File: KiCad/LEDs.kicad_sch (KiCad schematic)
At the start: 36 parts

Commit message: First production
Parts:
- gave numbers to parts that had none: 36

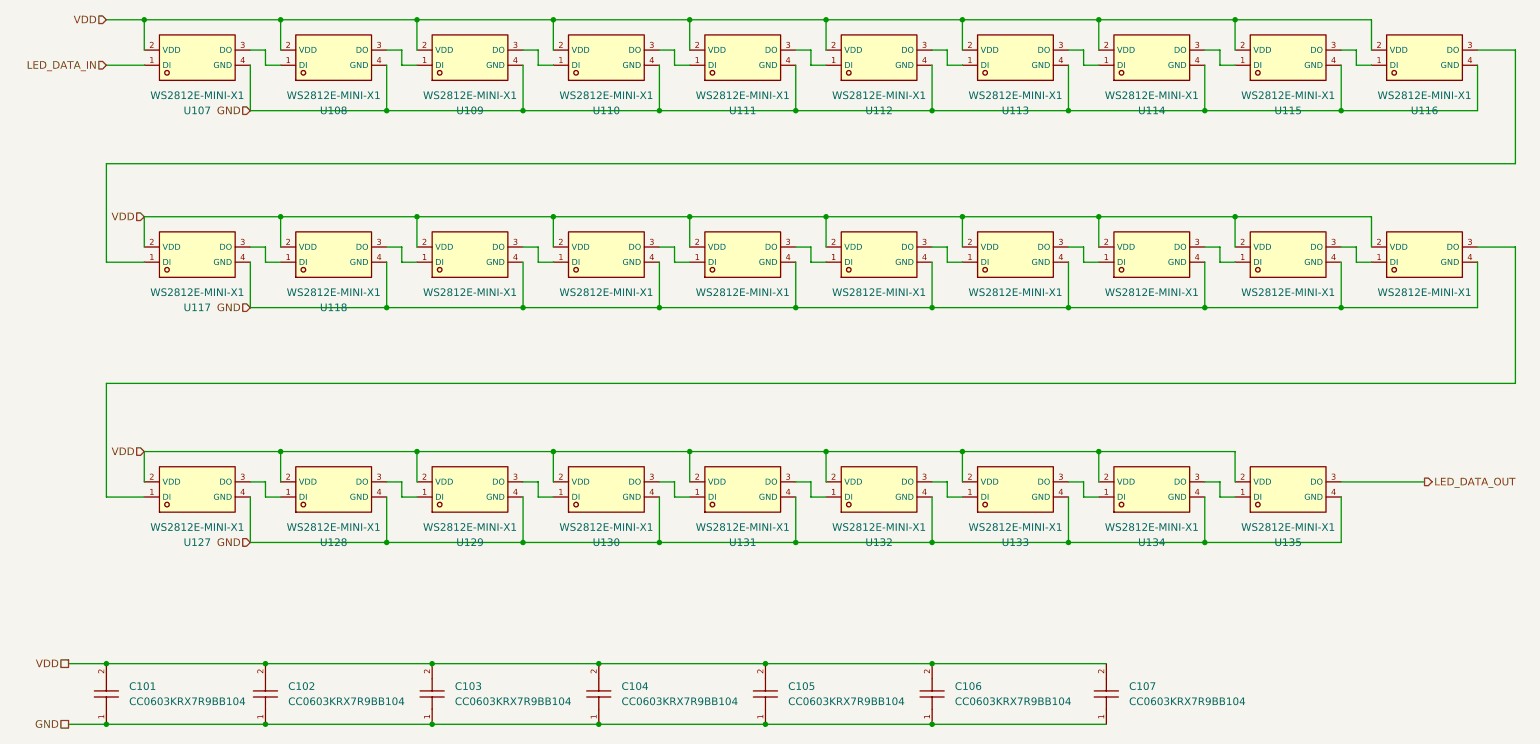
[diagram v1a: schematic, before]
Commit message: Updated to not use adressable LED. Sch only
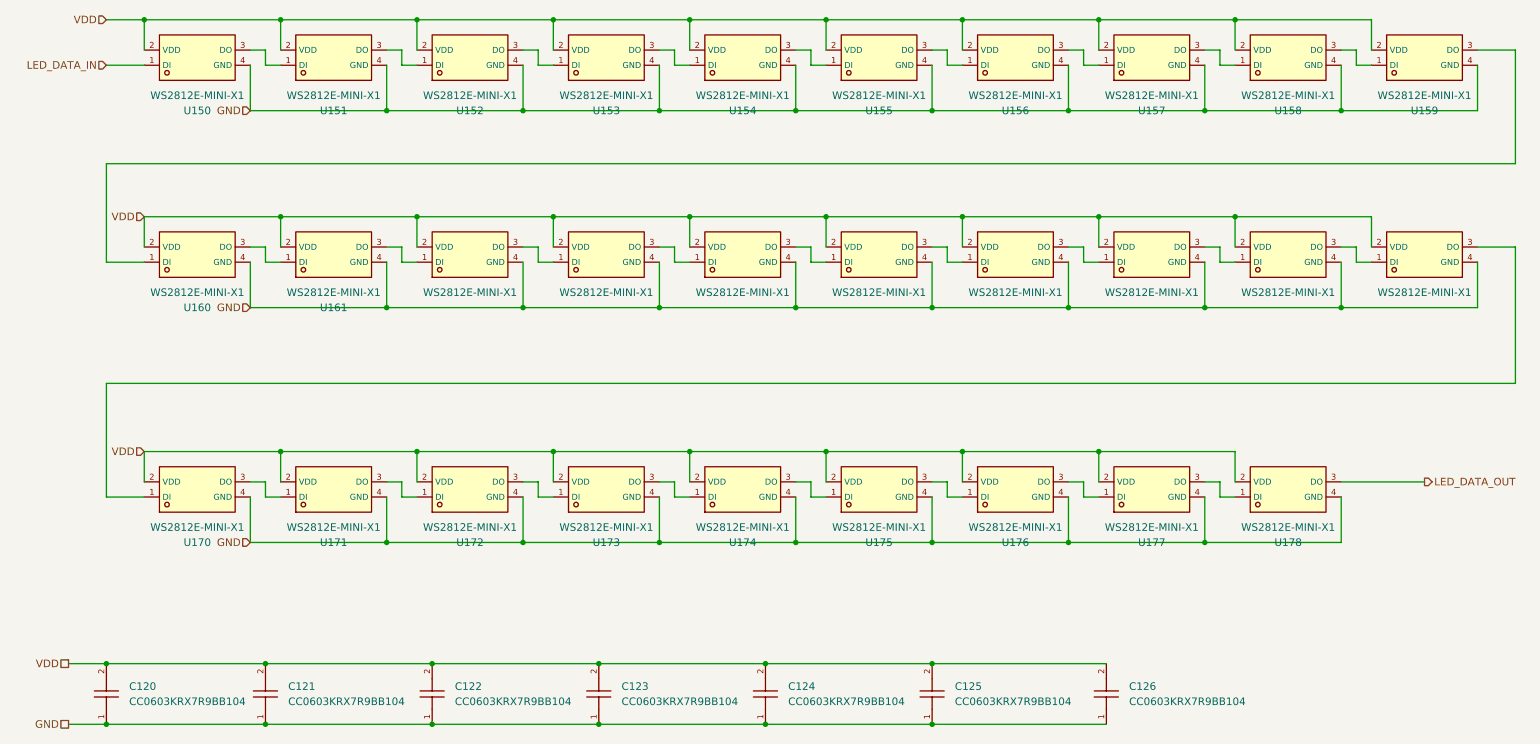
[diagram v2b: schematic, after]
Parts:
- renumbered C101 to C120, C102 to C121, C103 to C122, C104 to C123, C105 to C124, C106 to C125, C107 to C126, U107 to U150, U108 to U151, U109 to U152, U110 to U153, U111 to U154, U112 to U155, U113 to U156, U114 to U157, U115 to U158, U116 to U159, U117 to U160, U118 to U161, U119 to U162, U120 to U163, U121 to U164, U122 to U165, U123 to U166, U124 to U167, U125 to U168, U126 to U169, U127 to U170, U128 to U171, U129 to U172, U130 to U173, U131 to U174, U132 to U175, U133 to U176, U134 to U177, U135 to U178
